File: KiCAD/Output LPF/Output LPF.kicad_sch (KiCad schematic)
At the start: 67 parts, among them J1 Conn_Coaxial_Small, J2 8P8C_Shielded, J28 Filter In, K1 G6K-2P-Y-T1, K2 G6K-2P-Y-T1, K3 G6K-2P-Y-T1, K4 G6K-2P-Y-T1, Q1 2N7000, Q10 2N7000, Q5 2N7000, Q8 2N7000

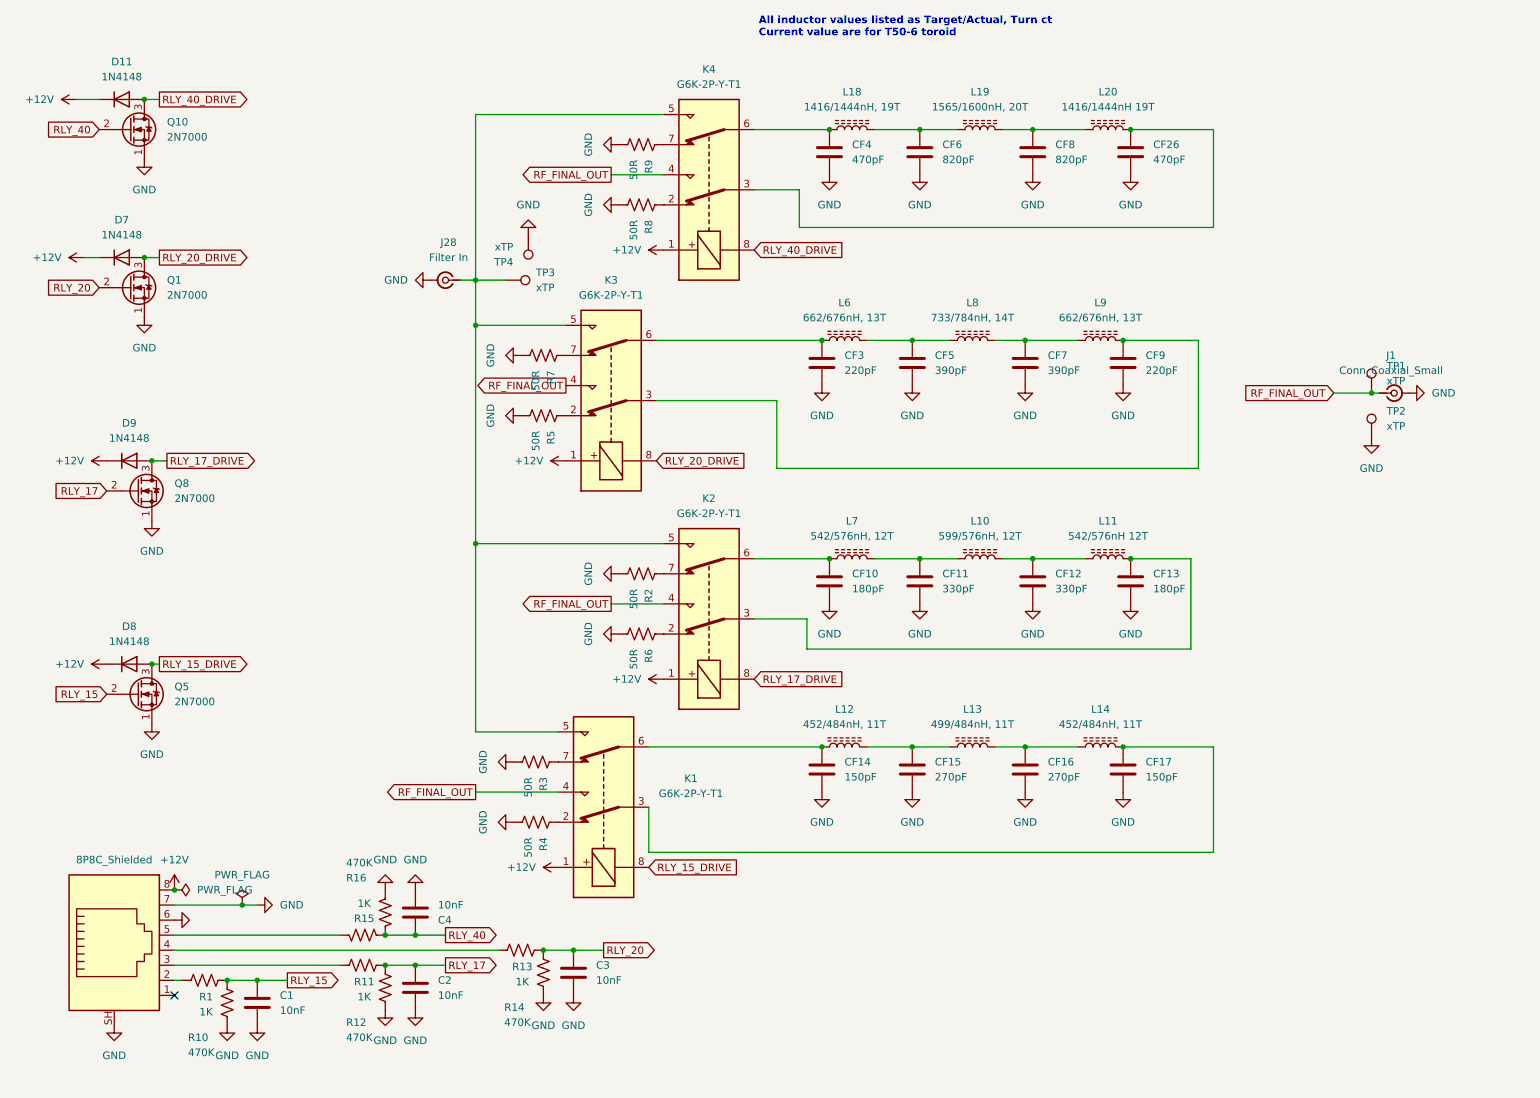
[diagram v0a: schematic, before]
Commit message: revD: Output LPF T/R relay + RX Schottky protection + sense sense-logic fix
Output LPF: K5 G6K DPDT T/R relay added at LPF output -- pole 2 switches
antenna (J1) between RF_FINAL_OUT (TX) and the RX protected port
(default/fail-safe RX). RX port protected by D1/D2 1N5711 antiparallel
Schottky clamp + R19 10R series fuse resistor into J3 SMA.

Pole 1 of K5 wired as negative-logic T/R status sense: K5 pin 3 (COM)
to GND, pin 2 (NC) carries RECEIVE_N, pin 4 (NO) carries TRANSMIT_N.
In each relay state, exactly one of {TRANSMIT_N, RECEIVE_N} is pulled
LOW (active) while the other sits HIGH via the PCF8575 internal pullup
on the analog side (U17 pins P0, P1). No external pulldowns required.

Analog: arduino.kicad_sch picks up the matching TRANSMIT_N / RECEIVE_N
and T/R RELAY drive wiring on the J2 (Output LPF umbilical) side.

Co-Authored-By: Claude Opus 4.7 <noreply@anthropic.com>
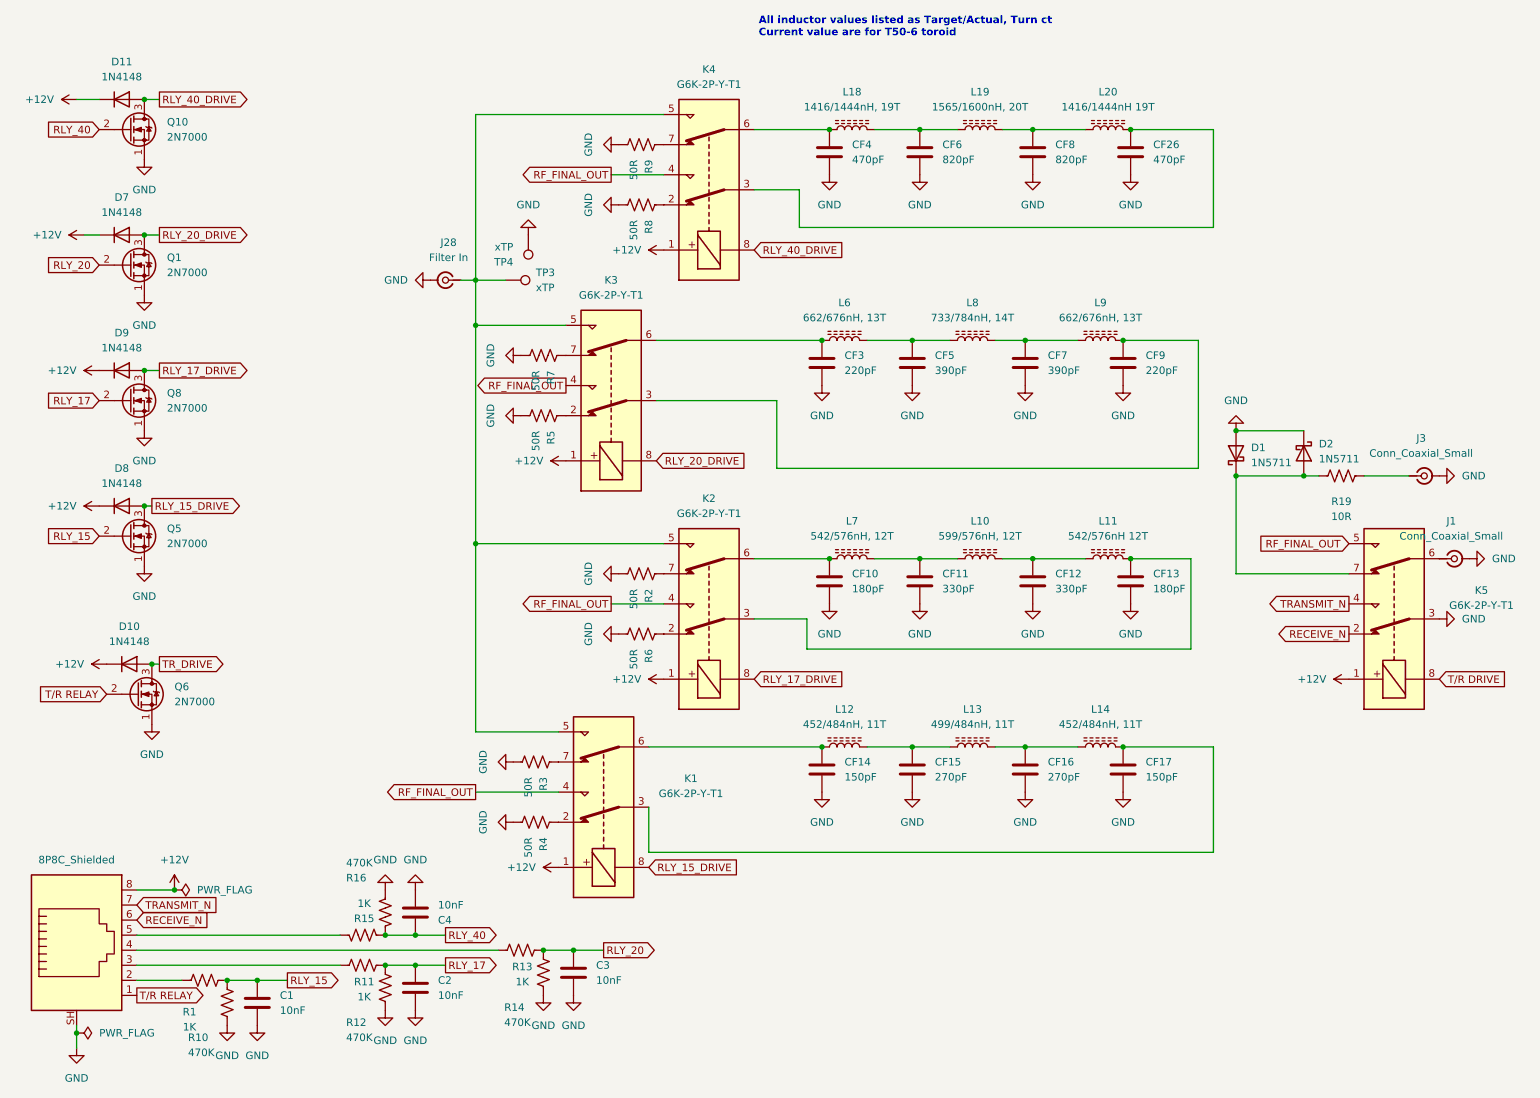
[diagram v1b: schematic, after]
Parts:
- removed TP1, TP2: xTP, Connector_PinHeader_2.54mm:PinHeader_1x01_P2.54mm_Vertical, symbol xmitter:xTP
- added D1, D2: 1N5711, Diode_THT:D_DO-35_SOD27_P7.62mm_Horizontal, symbol Diode:1N5711
- added D10: 1N4148, Diode_THT:D_DO-35_SOD27_P7.62mm_Horizontal, symbol Diode:1N4148
- added J3: Conn_Coaxial_Small, Connector_Coaxial:SMA_Amphenol_132134_Vertical, symbol Connector:Conn_Coaxial_Small
- added K5: G6K-2P-Y-T1, xmitter:Relay_DPDT_G6K-2P-Y-T1, symbol xmitter:Relay_G6K
- added Q6: 2N7000, Package_TO_SOT_THT:TO-92_Inline, symbol Transistor_FET:2N7000
- added R19: 10R, symbol Device:R_US
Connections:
- net +12V: now also D10.1 (K), K5.1
- net GND: now also D1.2 (A), D2.1 (K), J3.2 (Ext), K5.3, Q6.1 (S); no longer J2.6, J2.7
- net RF_FINAL_OUT: now also K5.5; no longer J1.1 (In)
- net T/R RELAY: now reaches J2.1
- net T/R RELAY: now also Q6.2 (G)
- new net: J1.1 (In), K5.6
- new net: D1.1 (K), D2.2 (A), K5.7, R19.1
- new net: J3.1 (In), R19.2
- new net RECEIVE_N: J2.6, K5.2
- new net TRANSMIT_N: J2.7, K5.4
- new net TR_DRIVE: D10.2 (A), Q6.3 (D)
- new net T/R DRIVE: K5.8
- no-connect marks 1 -> 0
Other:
- moved on the sheet: D7, D8, D9, J1, Q1, Q5, Q8

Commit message: revD: footprint pass across all boards + ss_pa fault-chain fix + LLM review brief
- New tools/assign_misc_footprints.py: lib_id-keyed footprint assigner
  (resistors, screw terminals, pin headers, LT1054); mirrors cap-script
  safe-write (UTF-8 no BOM, no CRLF translation).
- tools/assign_cap_footprints.py: added 0.47uF -> C_Rect_L7.0mm case.
- Ran both scripts across analog, ss_pa, Output LPF, frontpanel,
  protoshield, and shelved power board. ~100 fills; details in diffs.
- ss_pa: R1-R4 (0.22 ohm source sense) upgraded to 2W Yageo RSF200
  with DIN0516 L15.5mm/P20.32mm footprint; Value tagged "0.22R 2W".
  R15/R16 confirmed 1/4W (DIN0207) for BS170 source degeneration.
- analog/power: R44 15R 5W horizontal, P30.48mm footprint.
- ss_pa fault chain (from external LLM review): R21/R22 raised
  10K -> 100K to restore self-latching loop gain; new R26 = 100K
  across C12 so cap discharges between power cycles (reliable reset).
  R26 footprint pending.
- Documentation/revD_llm_review_brief.md: new, comprehensive system
  description for external LLM deep-dive (function, component values,
  power dissipation, design flaws). References all five board netlists.

Co-Authored-By: Claude Opus 4.7 <noreply@anthropic.com>
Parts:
- added C5, C6, C7, C8, C9: 10nF, Capacitor_THT:C_Disc_D6.0mm_W2.5mm_P5.00mm, symbol Device:C
- added R17, R18, R20, R21, R22: 10K, Resistor_THT:R_Axial_DIN0207_L6.3mm_D2.5mm_P10.16mm_Horizontal, symbol Device:R_US
- added R23, R24, R25, R26, R27: 470K, Resistor_THT:R_Axial_DIN0207_L6.3mm_D2.5mm_P10.16mm_Horizontal, symbol Device:R_US
- C1, C2, C3, C4: footprint (none) -> Capacitor_THT:C_Disc_D6.0mm_W2.5mm_P5.00mm
- R1, R10, R11, R12, R13, R14, R15, R16, R19: footprint (none) -> Resistor_THT:R_Axial_DIN0207_L6.3mm_D2.5mm_P10.16mm_Horizontal
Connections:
- net T/R DRIVE is gone; now on net T/R_DRIVE: K5.8
- net GND: now also C5.2, C6.2, C7.2, C8.2, C9.2, R23.2, R24.2, R25.2, R26.2, R27.2
- net RLY_15: now also R18.1; no longer Q5.2 (G)
- net RLY_17: now also R20.1; no longer Q8.2 (G)
- net RLY_20: now also R21.1; no longer Q1.2 (G)
- net RLY_40: now also R22.1; no longer Q10.2 (G)
- net T/R RELAY: now also R17.1; no longer Q6.2 (G)
- net TR_DRIVE renamed T/R_DRIVE
- new net: C9.1, Q10.2 (G), R22.2, R23.1
- new net: C7.1, Q8.2 (G), R20.2, R25.1
- new net: C6.1, Q5.2 (G), R18.2, R26.1
- new net: C5.1, Q6.2 (G), R17.2, R27.1
- new net: C8.1, Q1.2 (G), R21.2, R24.1
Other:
- moved on the sheet: D10, D11, D7, D8, D9, Q1, Q10, Q5, Q6, Q8
